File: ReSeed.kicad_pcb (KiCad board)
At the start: 2 copper layers, 60.8 x 99.9 mm, 47 parts, among them CN1 EDGE_CONNECTOR, CN2 AUDIO_OUT, CN3 AUDIO_IN, CN4 DB9_MALE, Q1 2SC1815, SW1 SW_DIGIFIX, U1 MOS_8580, U2 CD4520BE, U3 74LS245, U4 GAL16V8, U5 TL497ACN

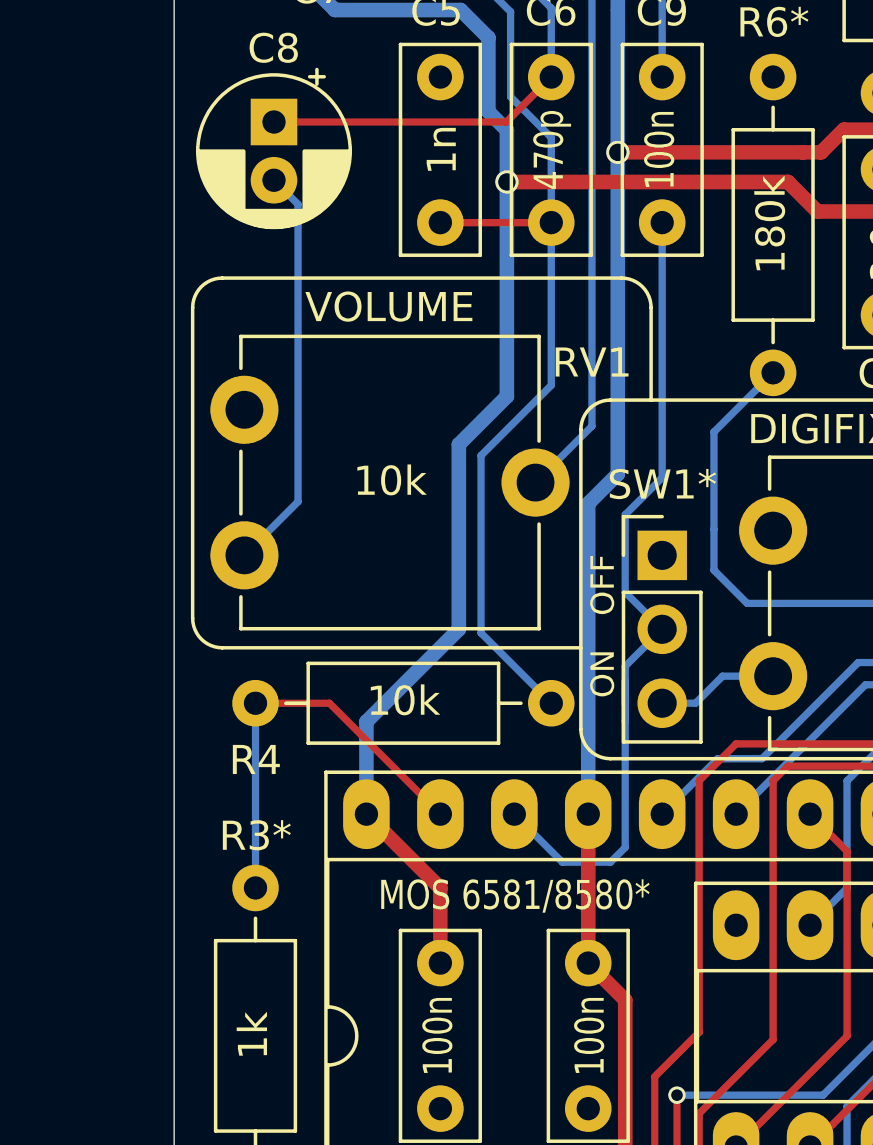
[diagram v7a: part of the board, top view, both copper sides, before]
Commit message: Reroute one more track to make ground more solid around DC-DC converter
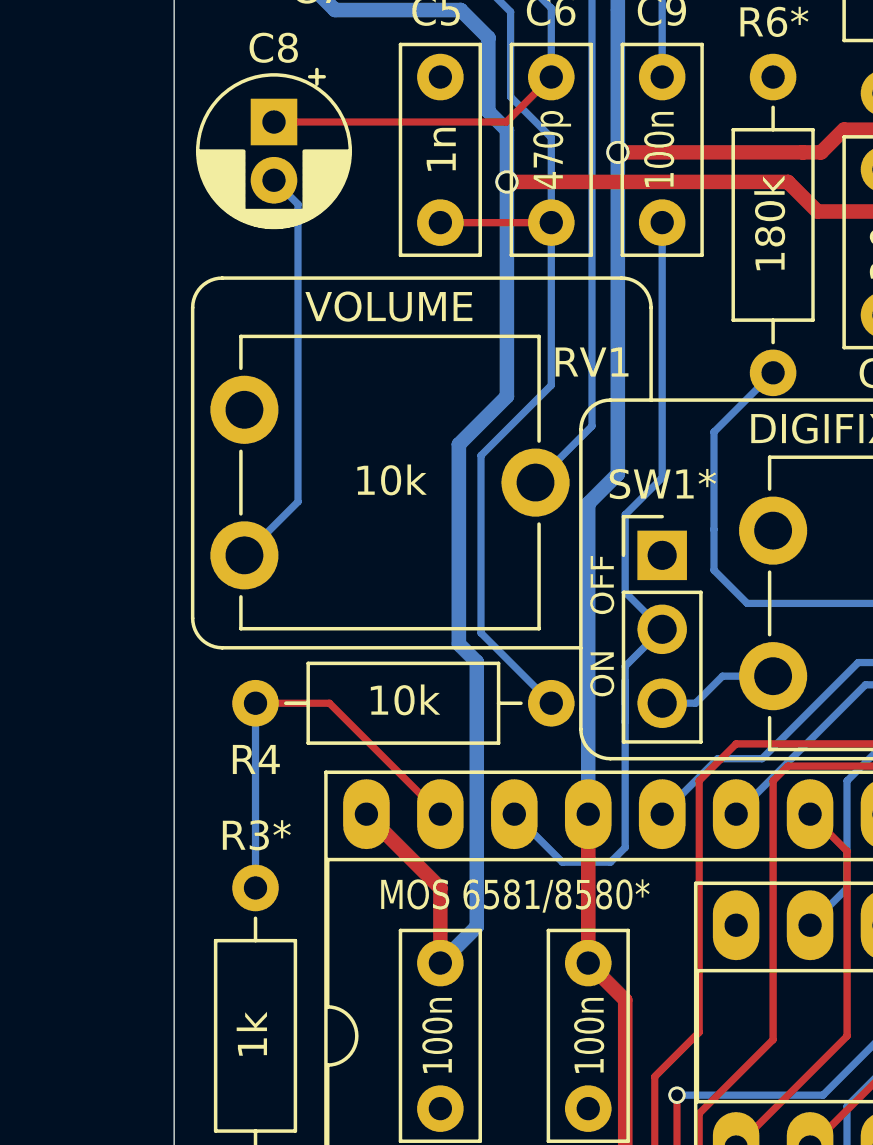
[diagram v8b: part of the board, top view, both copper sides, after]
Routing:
- net +9V: track 104.5 -> 109.1 mm
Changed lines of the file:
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@@
     (thickness 1.6)
     (drawings 45)
-    (tracks 609)
+    (tracks 610)
     (zones 0)
     (modules 47)
@@
   (title_block
     (title ReSeed)
-    (date 2022-03-05)
+    (date 2022-03-06)
     (rev 1git)
     (company SukkoPera)
@@
   (segment (start 123.952 68.199) (end 124.206 68.453) (width 0.5) (layer B.Cu) (net 8))
   (segment (start 123.952 66.275) (end 123.952 68.199) (width 0.5) (layer B.Cu) (net 8))
-  (segment (start 131.572 88.519) (end 133.223 86.868) (width 0.5) (layer B.Cu) (net 8))
   (segment (start 132.588 77.089) (end 132.588 74.549) (width 0.5) (layer B.Cu) (net 8))
   (segment (start 133.223 77.724) (end 132.588 77.089) (width 0.5) (layer B.Cu) (net 8))
@@
   (segment (start 127.3175 73.5965) (end 131.6355 73.5965) (width 0.5) (layer B.Cu) (net 8))
   (segment (start 124.206 70.485) (end 127.3175 73.5965) (width 0.5) (layer B.Cu) (net 8))
-  (segment (start 131.572 94.869) (end 131.572 88.519) (width 0.5) (layer B.Cu) (net 8))
-  (segment (start 128.397 98.044) (end 131.572 94.869) (width 0.5) (layer B.Cu) (net 8))
-  (segment (start 128.397 101.219) (end 128.397 98.044) (width 0.5) (layer B.Cu) (net 8))
   (via (at 133.223 79.502) (size 0.8) (drill 0.6) (layers F.Cu B.Cu) (net 8))
   (segment (start 133.223 79.502) (end 133.223 77.724) (width 0.5) (layer B.Cu) (net 8))
-  (segment (start 133.223 86.868) (end 133.223 79.502) (width 0.5) (layer B.Cu) (net 8))
   (segment (start 174.117 84.074) (end 174.117 84.709) (width 0.5) (layer F.Cu) (net 8))
   (segment (start 130.937 103.759) (end 128.397 101.219) (width 0.5) (layer F.Cu) (net 8))
@@
   (segment (start 164.084 89.916) (end 166.497 87.503) (width 0.5) (layer F.Cu) (net 8))
   (segment (start 159.639 89.916) (end 164.084 89.916) (width 0.5) (layer F.Cu) (net 8))
+  (segment (start 132.18701 105.08399) (end 130.937 106.334) (width 0.5) (layer B.Cu) (net 8))
+  (segment (start 132.18701 95.99201) (end 132.18701 105.08399) (width 0.5) (layer B.Cu) (net 8))
+  (segment (start 131.572 95.377) (end 132.18701 95.99201) (width 0.5) (layer B.Cu) (net 8))
+  (segment (start 131.572 88.519) (end 131.572 95.377) (width 0.5) (layer B.Cu) (net 8))
+  (segment (start 133.223 86.868) (end 131.572 88.519) (width 0.5) (layer B.Cu) (net 8))
+  (segment (start 133.223 79.502) (end 133.223 86.868) (width 0.5) (layer B.Cu) (net 8))
   (segment (start 132.177 144.018) (end 132.177 139.289) (width 0.5) (layer F.Cu) (net 9) (status 10))
   (segment (start 179.083 123.957) (end 179.083 126.497) (width 0.5) (layer F.Cu) (net 9) (status 30))
